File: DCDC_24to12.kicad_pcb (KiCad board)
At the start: 2 copper layers, 61.6 x 36.7 mm, 26 parts, among them J1 Power_IN, J2 Power_OUT, U1 BD9F800MUX-ZE2

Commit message: ノーテーション変更の反映
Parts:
- renumbered C5 to C4, C7 to C5, C4 to C6, C6 to C7, D4 to D3, D3 to D4, R3 to R1, R2 to R10, R4 to R2, R5 to R3, R6 to R4, R7 to R5, R8 to R6, R9 to R7, R1 to R8, R10 to R9
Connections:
- R4 pad 1: +12V -> FB
- R4 pad 2: FB -> +12V
- R5 pad 1: FB -> Net-(R5-Pad1)
- R5 pad 2: Net-(R7-Pad2) -> FB
- R6 pad 1: Net-(R7-Pad2) -> Net-(R6-Pad1)
- R6 pad 2: Net-(R8-Pad2) -> Net-(R5-Pad1)
- R7 pad 1: Net-(R8-Pad2) -> GND
- R7 pad 2: GND -> Net-(R6-Pad1)
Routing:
- net FB: track 5.01 -> 7.52 mm
- net Net-(R7-Pad2): track 2.03 -> 0.00 mm
- net Net-(R5-Pad1): track 0.00 -> 2.03 mm
- net Net-(R8-Pad2): track 2.03 -> 0.00 mm
- net Net-(R6-Pad1): track 0.00 -> 2.03 mm
- net +12V: track 36.6 -> 37.5 mm

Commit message: 穴追加
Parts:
- added H1: MountingHole_Pad, MountingHole:MountingHole_3.2mm_M3_Pad_Via, F.Cu at (75.3, 72.0)
- added H2: MountingHole_Pad, MountingHole:MountingHole_3.2mm_M3_Pad_Via, F.Cu at (128.9, 43.2)
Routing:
- net GND: vias 117 -> 108

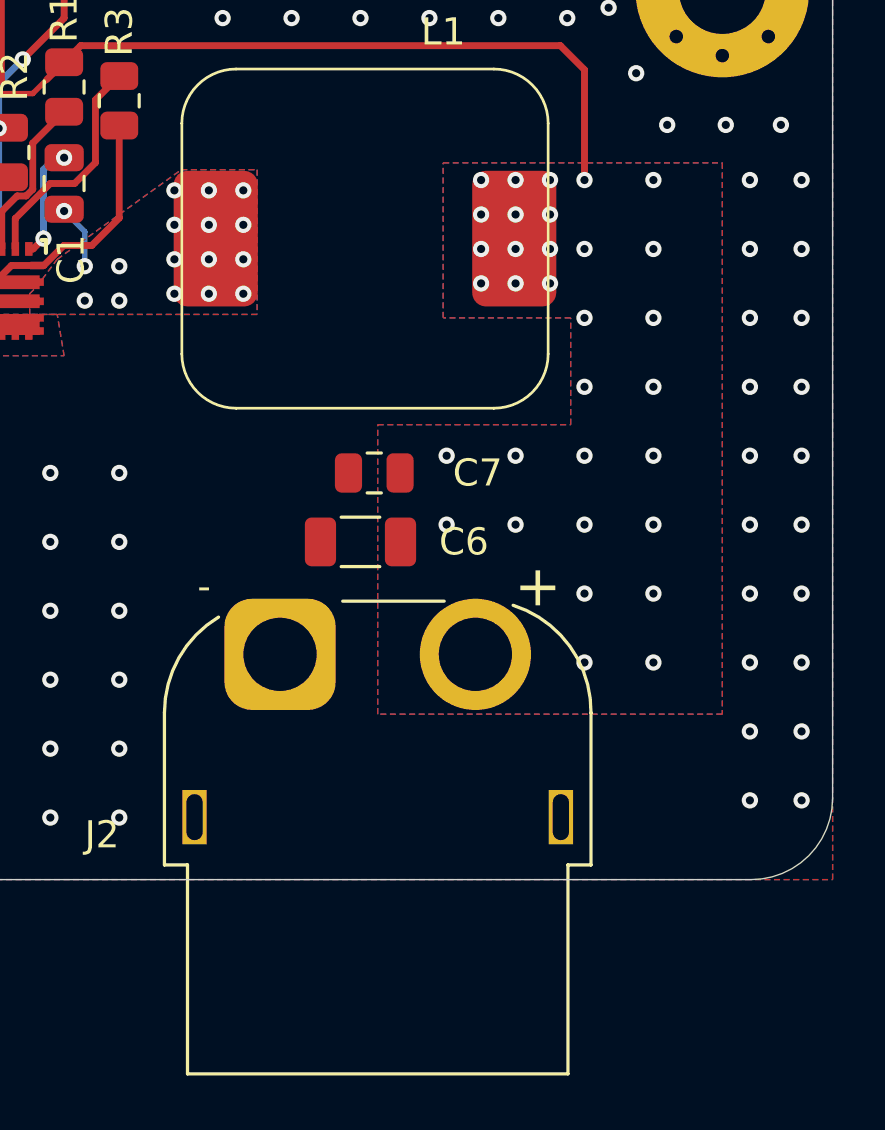
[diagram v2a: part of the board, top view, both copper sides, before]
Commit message: 出力コネクタをタテにした
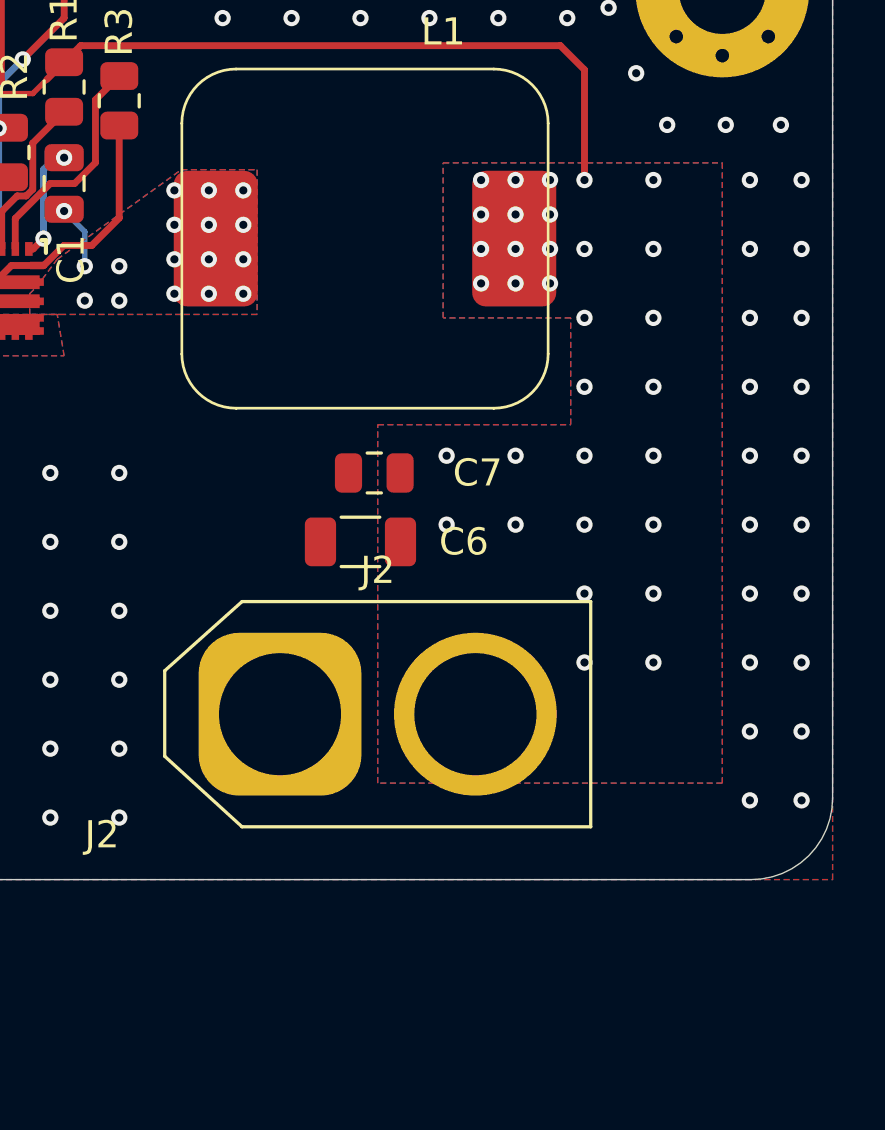
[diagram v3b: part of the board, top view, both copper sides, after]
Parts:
- J2: footprint Connector_AMASS:AMASS_XT60PW-F_1x02_P7.20mm_Horizontal -> Connector_AMASS:AMASS_XT60-F_1x02_P7.20mm_Vertical
- moved J2 2.20 mm to (112.6, 69.8), turned to 0 degrees
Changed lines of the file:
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@@
 		)
 	)
-	(footprint "Connector_AMASS:AMASS_XT60PW-F_1x02_P7.20mm_Horizontal"
+	(footprint "Connector_AMASS:AMASS_XT60-F_1x02_P7.20mm_Vertical"
 		(layer "F.Cu")
-		(at 112.605 67.645 180)
-		(descr "Connector XT60 Horizontal PCB Female, https://www.tme.eu/en/Document/9b8d0c5eb7094295f3d3112c214d3ade/XT60PW%20SPEC.pdf")
-		(tags "RC Connector XT60")
+		(at 112.605 69.85)
+		(descr "AMASS female XT60, through hole, vertical, https://www.tme.eu/Document/2d152ced3b7a446066e6c419d84bb460/XT60%20SPEC.pdf")
+		(tags "XT60 female vertical")
 		(property "Reference" "J2"
-			(at 3.766 3.637 0)
+			(at 3.6 -5.3 360)
 			(layer "F.SilkS")
-			(hide yes)
 			(effects
 				(font
@@
 		)
 		(property "Value" "Power_OUT"
-			(at -3.6 4 0)
+			(at 3.6 5.4 360)
 			(layer "F.Fab")
 			(effects
@@
 			)
 		)
-		(property "Footprint" "Connector_AMASS:AMASS_XT60PW-F_1x02_P7.20mm_Horizontal"
-			(at 0 0 180)
+		(property "Footprint" "Connector_AMASS:AMASS_XT60-F_1x02_P7.20mm_Vertical"
+			(at 0 0 0)
 			(unlocked yes)
 			(layer "F.Fab")
@@
 		)
 		(property "Datasheet" ""
-			(at 0 0 180)
+			(at 0 0 0)
 			(unlocked yes)
 			(layer "F.Fab")
@@
 		)
 		(property "Description" "Generic connector, single row, 01x02, script generated"
-			(at 0 0 180)
+			(at 0 0 0)
 			(unlocked yes)
 			(layer "F.Fab")
@@
 		(attr through_hole)
 		(fp_line
-			(start 4.26 -7.76)
-			(end 4.26 -2.15)
-			(stroke
-				(width 0.12)
-				(type solid)
-			)
-			(layer "F.SilkS")
-		)
-		(fp_line
-			(start 3.41 -7.76)
-			(end 4.26 -7.76)
+			(start -4.25 -1.6)
+			(end -4.25 1.55)
 			(stroke
 				(width 0.12)
@@
 		)
 		(fp_line
-			(start 3.41 -15.46)
-			(end 3.41 -7.76)
+			(start -4.25 1.55)
+			(end -1.4 4.15)
 			(stroke
 				(width 0.12)
@@
 		)
 		(fp_line
-			(start -6.05 1.96)
-			(end -2.31 1.96)
+			(start -1.4 -4.15)
+			(end -4.25 -1.6)
 			(stroke
 				(width 0.12)
@@
 		)
 		(fp_line
-			(start -10.61 -15.46)
-			(end 3.41 -15.46)
+			(start -1.4 4.15)
+			(end 11.45 4.15)
 			(stroke
 				(width 0.12)
@@
 		)
 		(fp_line
-			(start -10.61 -15.46)
-			(end -10.61 -7.76)
+			(start 11.45 -4.15)
+			(end -1.4 -4.15)
 			(stroke
 				(width 0.12)
@@
 		)
 		(fp_line
-			(start -11.46 -7.76)
-			(end -10.61 -7.76)
+			(start 11.45 4.15)
+			(end 11.45 -4.15)
 			(stroke
 				(width 0.12)
@@
 		)
 		(fp_line
-			(start -11.46 -7.76)
-			(end -11.46 -2.15)
+			(start -4.65 -1.85)
+			(end -1.6 -4.6)
 			(stroke
-				(width 0.12)
-				(type solid)
-			)
-			(layer "F.SilkS")
-		)
-		(fp_arc
-			(start 4.26 -2.15)
-			(mid 3.727162 -0.126139)
-			(end 2.266806 1.372958)
-			(stroke
-				(width 0.12)
-				(type solid)
-			)
-			(layer "F.SilkS")
-		)
-		(fp_arc
-			(start -8.5899 1.808718)
-			(mid -10.677645 0.302568)
-			(end -11.46 -2.15)
-			(stroke
-				(width 0.12)
+				(width 0.05)
 				(type solid)
 			)
-			(layer "F.SilkS")
+			(layer "F.CrtYd")
 		)
 		(fp_line
-			(start 4.65 2.55)
-			(end 4.65 -15.85)
+			(start -4.65 1.85)
+			(end -4.65 -1.85)
 			(stroke
 				(width 0.05)
@@
 		)
 		(fp_line
-			(start 4.65 2.55)
-			(end -11.85 2.55)
+			(start -1.6 -4.6)
+			(end 11.85 -4.6)
 			(stroke
 				(width 0.05)
@@
 		)
 		(fp_line
-			(start -11.85 -15.85)
-			(end 4.65 -15.85)
+			(start -1.6 4.6)
+			(end -4.65 1.85)
 			(stroke
 				(width 0.05)
@@
 		)
 		(fp_line
-			(start -11.85 -15.85)
-			(end -11.85 2.55)
+			(start 11.85 -4.6)
+			(end 11.85 4.6)
 			(stroke
 				(width 0.05)
@@
 		)
 		(fp_line
-			(start 4.15 -7.65)
-			(end 4.15 -2.15)
+			(start 11.85 4.6)
+			(end -1.6 4.6)
 			(stroke
-				(width 0.1)
+				(width 0.05)
 				(type solid)
 			)
-			(layer "F.Fab")
+			(layer "F.CrtYd")
 		)
 		(fp_line
-			(start 3.3 -7.65)
-			(end 3.3 -15.35)
+			(start -4.15 -1.55)
+			(end -4.15 1.55)
 			(stroke
-				(width 0.1)
+				(width 0.12)
 				(type solid)
 			)
@@
 		)
 		(fp_line
-			(start -7.35 1.85)
-			(end 0.15 1.85)
+			(start -4.15 1.55)
+			(end -1.4 4.05)
 			(stroke
-				(width 0.1)
+				(width 0.12)
 				(type solid)
 			)
@@
 		)
 		(fp_line
-			(start -10.5 -7.65)
-			(end -10.5 -15.35)
+			(start -1.4 -4.05)
+			(end -4.15 -1.55)
 			(stroke
-				(width 0.1)
+				(width 0.12)
 				(type solid)
 			)
@@
 		)
 		(fp_line
-			(start -10.5 -15.35)
-			(end 3.3 -15.35)
+			(start -1.4 4.05)
+			(end 11.35 4.05)
 			(stroke
-				(width 0.1)
+				(width 0.12)
 				(type solid)
 			)
@@
 		)
 		(fp_line
-			(start -11.35 -7.65)
-			(end 4.15 -7.65)
+			(start 11.35 -4.05)
+			(end -1.4 -4.05)
 			(stroke
-				(width 0.1)
+				(width 0.12)
 				(type solid)
 			)
@@
 		)
 		(fp_line
-			(start -11.35 -7.65)
-			(end -11.35 -2.15)
+			(start 11.35 4.05)
+			(end 11.35 -4.05)
 			(stroke
-				(width 0.1)
-				(type solid)
-			)
-			(layer "F.Fab")
-		)
-		(fp_arc
-			(start 4.15 -2.15)
-			(mid 2.978427 0.678427)
-			(end 0.15 1.85)
-			(stroke
-				(width 0.1)
-				(type solid)
-			)
-			(layer "F.Fab")
-		)
-		(fp_arc
-			(start -7.385 1.885)
-			(mid -10.203176 0.688678)
-			(end -11.35 -2.15)
-			(stroke
-				(width 0.1)
+				(width 0.12)
 				(type solid)
 			)
 			(layer "F.Fab")
 		)
-		(fp_text user "+"
-			(at -9.5 2.5 0)
-			(layer "F.SilkS")
-			(effects
-				(font
-					(size 1.5 1.5)
-					(thickness 0.15)
-				)
-			)
-		)
-		(fp_text user "-"
-			(at 2.8 2.5 0)
-			(layer "F.SilkS")
-			(effects
-				(font
-					(size 1 1)
-					(thickness 0.15)
-				)
-			)
-		)
 		(fp_text user "${REFERENCE}"
-			(at -3.6 -3.6 0)
+			(at 3.6 0.05 360)
 			(layer "F.Fab")
 			(effects
@@
 			)
 		)
-		(pad "" thru_hole rect
-			(at -10.35 -6 180)
-			(size 0.9 2)
-			(drill oval 0.6 1.7)
-			(layers "*.Cu" "*.Mask")
-			(remove_unused_layers no)
-		)
-		(pad "" thru_hole rect
-			(at 3.15 -6 180)
-			(size 0.9 2)
-			(drill oval 0.6 1.7)
-			(layers "*.Cu" "*.Mask")
-			(remove_unused_layers no)
-		)
 		(pad "1" thru_hole roundrect
-			(at 0 0 180)
-			(size 4.1 4.1)
-			(drill 2.7)
+			(at 0 0)
+			(size 6 6)
+			(drill 4.5)
 			(layers "*.Cu" "*.Mask")
 			(remove_unused_layers no)
@@
 		)
 		(pad "2" thru_hole circle
-			(at -7.2 0 180)
-			(size 4.1 4.1)
-			(drill 2.7)
+			(at 7.2 0)
+			(size 6 6)
+			(drill 4.5)
 			(layers "*.Cu" "*.Mask")
 			(remove_unused_layers no)
@@
 			(pintype "passive")
 		)
-		(model "${KICAD8_3DMODEL_DIR}/Connector_AMASS.3dshapes/AMASS_XT60PW-F_1x02_P7.20mm_Horizontal.wrl"
+		(model "${KICAD8_3DMODEL_DIR}/Connector_AMASS.3dshapes/AMASS_XT60-F_1x02_P7.2mm_Vertical.wrl"
 			(offset
 				(xyz 0 0 0)
@@
 	)
 	(gr_rect
-		(start 109.855 64.77)
-		(end 115.189 70.231)
+		(start 108.839 66.167)
+		(end 115.824 73.787)
 		(stroke
 			(width 0.1)
@@
 	)
 	(gr_rect
-		(start 117.475 64.77)
-		(end 122.555 69.85)
+		(start 116.713 66.04)
+		(end 123.698 72.39)
 		(stroke
 			(width 0.1)
@@
 		(polygon
 			(pts
-				(xy 116.205 69.85) (xy 116.205 59.182) (xy 123.317 59.182) (xy 123.317 55.245) (xy 118.618 55.245)
-				(xy 118.618 49.53) (xy 128.905 49.53) (xy 128.905 69.85)
+				(xy 116.205 72.39) (xy 116.205 59.182) (xy 123.317 59.182) (xy 123.317 55.245) (xy 118.618 55.245)
+				(xy 118.618 49.53) (xy 128.905 49.53) (xy 128.905 72.39)
 			)
 		)

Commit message: だいぶ小型化
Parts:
- moved J2 23.9 mm to (89.0, 66.0)
- moved C6 14.6 mm to (102.9, 70.7), turned to -90 degrees
- moved C7 14.5 mm to (105.4, 70.8), turned to -90 degrees
- moved H2 12.1 mm to (116.8, 43.2)
- moved L1 2.26 mm to (111.6, 54.1), turned to -90 degrees
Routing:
- net +12V: track 37.5 -> 40.5 mm, vias 32 -> 8
- net SW: vias 17 -> 15
- net GND: vias 108 -> 28
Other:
- board outline removed
